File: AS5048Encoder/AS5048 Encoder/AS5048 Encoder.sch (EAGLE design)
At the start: 5 parts, among them X1 SI-50170

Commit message: all parts in place
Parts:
- added TP1, TP2, TP3, TP4, TP5: TPPAD1-17, testpad:TPPAD1-17
- added U$2: AS5145, makesmith:AS5145
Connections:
- new net N$10: X1.NC
- new net N$11: X1.C_GND
- new net N$2: U$2.CSN
- new net N$3: U$2.CLK
- new net N$4: U$2.DO
- new net N$9: X1.RD-
- new net SIG_A: TP4.TP, U$2.DTEST1A, X1.RD+
- new net SIG_B: TP5.TP, U$2.DTEST2B, X1.RCT
- net GND: now also TP2.TP
- net PWM: now also TP3.TP, U$2.PWM
- net VCC: now also TP1.TP
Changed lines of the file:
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@@
 <layer number="54" name="bGND_GNDA" color="1" fill="9" visible="no" active="no"/>
 <layer number="56" name="wert" color="7" fill="1" visible="no" active="no"/>
+<layer number="90" name="Modules" color="5" fill="1" visible="yes" active="yes"/>
 <layer number="91" name="Nets" color="2" fill="1" visible="yes" active="yes"/>
 <layer number="92" name="Busses" color="1" fill="1" visible="yes" active="yes"/>
@@
 <part name="U$1" library="austriamicrosystems" deviceset="AS5048" device=""/>
 <part name="X1" library="con-stewart" deviceset="SI-50170" device=""/>
+<part name="U$2" library="makesmith" deviceset="AS5145" device=""/>
+<part name="TP1" library="testpad" deviceset="TP" device="PAD1-17"/>
+<part name="TP2" library="testpad" deviceset="TP" device="PAD1-17"/>
+<part name="TP3" library="testpad" deviceset="TP" device="PAD1-17"/>
+<part name="TP4" library="testpad" deviceset="TP" device="PAD1-17"/>
+<part name="TP5" library="testpad" deviceset="TP" device="PAD1-17"/>
 </parts>
 <sheets>
@@
 <instance part="U$1" gate="G$1" x="66.04" y="25.4"/>
 <instance part="X1" gate="G$1" x="66.04" y="-7.62"/>
+<instance part="U$2" gate="G$1" x="-43.18" y="12.7"/>
+<instance part="TP1" gate="G$1" x="-38.1" y="63.5"/>
+<instance part="TP2" gate="G$1" x="-25.4" y="63.5"/>
+<instance part="TP3" gate="G$1" x="-12.7" y="63.5"/>
+<instance part="TP4" gate="G$1" x="-2.54" y="63.5"/>
+<instance part="TP5" gate="G$1" x="5.08" y="63.5"/>
 </instances>
 <busses>
@@
 <label x="48.26" y="2.54" size="1.778" layer="95"/>
 </segment>
+<segment>
+<pinref part="TP2" gate="G$1" pin="TP"/>
+<wire x1="-25.4" y1="60.96" x2="-25.4" y2="55.88" width="0.1524" layer="91"/>
+<label x="-25.4" y="55.88" size="1.778" layer="95" rot="R90"/>
+</segment>
 </net>
 <net name="VCC" class="0">
@@
 <label x="48.26" y="7.62" size="1.778" layer="95"/>
 </segment>
+<segment>
+<pinref part="TP1" gate="G$1" pin="TP"/>
+<wire x1="-38.1" y1="60.96" x2="-38.1" y2="55.88" width="0.1524" layer="91"/>
+<label x="-38.1" y="55.88" size="1.778" layer="95" rot="R90"/>
+</segment>
 </net>
 <net name="3V3" class="0">
@@
 <label x="48.26" y="5.08" size="1.778" layer="95"/>
 </segment>
-</net>
+<segment>
+<pinref part="U$2" gate="G$1" pin="PWM"/>
+<wire x1="-17.78" y1="5.08" x2="-12.7" y2="5.08" width="0.1524" layer="91"/>
+<label x="-12.7" y="5.08" size="1.778" layer="95"/>
+</segment>
+<segment>
+<pinref part="TP3" gate="G$1" pin="TP"/>
+<wire x1="-12.7" y1="60.96" x2="-12.7" y2="55.88" width="0.1524" layer="91"/>
+<label x="-12.7" y="55.88" size="1.778" layer="95" rot="R90"/>
+</segment>
+</net>
+<net name="N$2" class="0">
+<segment>
+<pinref part="U$2" gate="G$1" pin="CSN"/>
+<wire x1="-17.78" y1="0" x2="-12.7" y2="0" width="0.1524" layer="91"/>
+</segment>
+</net>
+<net name="N$3" class="0">
+<segment>
+<pinref part="U$2" gate="G$1" pin="CLK"/>
+<wire x1="-17.78" y1="-5.08" x2="-12.7" y2="-5.08" width="0.1524" layer="91"/>
+</segment>
+</net>
+<net name="N$4" class="0">
+<segment>
+<pinref part="U$2" gate="G$1" pin="DO"/>
+<wire x1="-17.78" y1="-10.16" x2="-12.7" y2="-10.16" width="0.1524" layer="91"/>
+</segment>
+</net>
+<net name="SIG_A" class="0">
+<segment>
+<pinref part="U$2" gate="G$1" pin="DTEST1A"/>
+<wire x1="-63.5" y1="15.24" x2="-68.58" y2="15.24" width="0.1524" layer="91"/>
+<label x="-73.66" y="15.24" size="1.778" layer="95"/>
+</segment>
+<segment>
+<pinref part="X1" gate="G$1" pin="RD+"/>
+<wire x1="55.88" y1="0" x2="53.34" y2="0" width="0.1524" layer="91"/>
+<label x="45.72" y="0" size="1.778" layer="95"/>
+</segment>
+<segment>
+<pinref part="TP4" gate="G$1" pin="TP"/>
+<wire x1="-2.54" y1="60.96" x2="-2.54" y2="55.88" width="0.1524" layer="91"/>
+<label x="-2.54" y="53.34" size="1.778" layer="95" rot="R90"/>
+</segment>
+</net>
+<net name="SIG_B" class="0">
+<segment>
+<pinref part="U$2" gate="G$1" pin="DTEST2B"/>
+<wire x1="-63.5" y1="10.16" x2="-68.58" y2="10.16" width="0.1524" layer="91"/>
+<label x="-73.66" y="10.16" size="1.778" layer="95"/>
+</segment>
+<segment>
+<pinref part="X1" gate="G$1" pin="RCT"/>
+<wire x1="55.88" y1="-2.54" x2="53.34" y2="-2.54" width="0.1524" layer="91"/>
+<label x="45.72" y="-2.54" size="1.778" layer="95"/>
+</segment>
+<segment>
+<pinref part="TP5" gate="G$1" pin="TP"/>
+<wire x1="5.08" y1="60.96" x2="5.08" y2="55.88" width="0.1524" layer="91"/>
+<label x="5.08" y="53.34" size="1.778" layer="95" rot="R90"/>
+</segment>
+</net>
+<net name="N$9" class="0">
+<segment>
+<pinref part="X1" gate="G$1" pin="RD-"/>
+<wire x1="55.88" y1="-5.08" x2="53.34" y2="-5.08" width="0.1524" layer="91"/>
+</segment>
+</net>
+<net name="N$10" class="0">
+<segment>
+<pinref part="X1" gate="G$1" pin="NC"/>
+<wire x1="55.88" y1="-7.62" x2="53.34" y2="-7.62" width="0.1524" layer="91"/>
+</segment>
+</net>
+<net name="N$11" class="0">
+<segment>
+<pinref part="X1" gate="G$1" pin="C_GND"/>
+<wire x1="55.88" y1="-10.16" x2="53.34" y2="-10.16" width="0.1524" layer="91"/>
+</segment>
+</net>

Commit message: board looks done?
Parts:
- removed U$1: AS5048, austriamicrosystems:AS5048
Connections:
- removed net N$10: X1.NC
- removed net N$11: X1.C_GND
- removed net N$9: X1.RD-
- net 3V3: now also U$2.VDD3V3; no longer U$1.3V3
- net GND: now also X1.NC; no longer U$1.GND, X1.TD-
- net PWM: now also X1.C_GND; no longer U$1.PWM, X1.TCT
- net SIG_A: now also X1.TCT; no longer X1.RD+
- net SIG_B: now also X1.TD+; no longer X1.RCT
- net VCC: now also U$2.VDD5V, X1.RD-; no longer U$1.5V, X1.TD+
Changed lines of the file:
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@@
 <part name="SUPPLY6" library="SparkFun-Aesthetics" deviceset="VCC" device=""/>
 <part name="JP1" library="SparkFun-Connectors" deviceset="M03" device="LOCK"/>
-<part name="U$1" library="austriamicrosystems" deviceset="AS5048" device=""/>
 <part name="X1" library="con-stewart" deviceset="SI-50170" device=""/>
 <part name="U$2" library="makesmith" deviceset="AS5145" device=""/>
@@
 <instance part="SUPPLY6" gate="1" x="12.7" y="27.94"/>
 <instance part="JP1" gate="G$1" x="63.5" y="58.42" rot="R270"/>
-<instance part="U$1" gate="G$1" x="66.04" y="25.4"/>
 <instance part="X1" gate="G$1" x="66.04" y="-7.62"/>
 <instance part="U$2" gate="G$1" x="-43.18" y="12.7"/>
@@
 </segment>
 <segment>
-<wire x1="53.34" y1="20.32" x2="50.8" y2="20.32" width="0.1524" layer="91"/>
-<label x="45.72" y="20.32" size="1.778" layer="95"/>
-<pinref part="U$1" gate="G$1" pin="GND"/>
-</segment>
-<segment>
 <pinref part="JP1" gate="G$1" pin="1"/>
 <wire x1="60.96" y1="50.8" x2="60.96" y2="45.72" width="0.1524" layer="91"/>
@@
 </segment>
 <segment>
-<pinref part="X1" gate="G$1" pin="TD-"/>
-<wire x1="55.88" y1="2.54" x2="53.34" y2="2.54" width="0.1524" layer="91"/>
-<label x="48.26" y="2.54" size="1.778" layer="95"/>
-</segment>
-<segment>
 <pinref part="TP2" gate="G$1" pin="TP"/>
 <wire x1="-25.4" y1="60.96" x2="-25.4" y2="55.88" width="0.1524" layer="91"/>
 <label x="-25.4" y="55.88" size="1.778" layer="95" rot="R90"/>
+</segment>
+<segment>
+<pinref part="X1" gate="G$1" pin="NC"/>
+<wire x1="55.88" y1="-7.62" x2="53.34" y2="-7.62" width="0.1524" layer="91"/>
+<label x="48.26" y="-7.62" size="1.778" layer="95"/>
 </segment>
 </net>
@@
 </segment>
 <segment>
-<wire x1="53.34" y1="30.48" x2="50.8" y2="30.48" width="0.1524" layer="91"/>
-<label x="45.72" y="30.48" size="1.778" layer="95"/>
-<pinref part="U$1" gate="G$1" pin="5V"/>
-</segment>
-<segment>
 <pinref part="JP1" gate="G$1" pin="2"/>
 <wire x1="63.5" y1="50.8" x2="63.5" y2="45.72" width="0.1524" layer="91"/>
@@
 </segment>
 <segment>
-<pinref part="X1" gate="G$1" pin="TD+"/>
-<wire x1="55.88" y1="7.62" x2="53.34" y2="7.62" width="0.1524" layer="91"/>
-<label x="48.26" y="7.62" size="1.778" layer="95"/>
-</segment>
-<segment>
 <pinref part="TP1" gate="G$1" pin="TP"/>
 <wire x1="-38.1" y1="60.96" x2="-38.1" y2="55.88" width="0.1524" layer="91"/>
 <label x="-38.1" y="55.88" size="1.778" layer="95" rot="R90"/>
+</segment>
+<segment>
+<pinref part="U$2" gate="G$1" pin="VDD5V"/>
+<wire x1="-17.78" y1="25.4" x2="-15.24" y2="25.4" width="0.1524" layer="91"/>
+<label x="-15.24" y="25.4" size="1.778" layer="95"/>
+</segment>
+<segment>
+<pinref part="X1" gate="G$1" pin="RD-"/>
+<wire x1="55.88" y1="-5.08" x2="53.34" y2="-5.08" width="0.1524" layer="91"/>
+<label x="48.26" y="-5.08" size="1.778" layer="95"/>
 </segment>
 </net>
@@
 </segment>
 <segment>
-<wire x1="53.34" y1="25.4" x2="50.8" y2="25.4" width="0.1524" layer="91"/>
-<label x="45.72" y="25.4" size="1.778" layer="95"/>
-<pinref part="U$1" gate="G$1" pin="3V3"/>
+<pinref part="U$2" gate="G$1" pin="VDD3V3"/>
+<wire x1="-17.78" y1="20.32" x2="-15.24" y2="20.32" width="0.1524" layer="91"/>
+<label x="-15.24" y="20.32" size="1.778" layer="95"/>
 </segment>
 </net>
 <net name="PWM" class="0">
 <segment>
-<label x="83.82" y="27.94" size="1.778" layer="95"/>
-<pinref part="U$1" gate="G$1" pin="PWM"/>
-<wire x1="81.28" y1="27.94" x2="83.82" y2="27.94" width="0.1524" layer="91"/>
-</segment>
-<segment>
 <pinref part="JP1" gate="G$1" pin="3"/>
 <wire x1="66.04" y1="50.8" x2="66.04" y2="45.72" width="0.1524" layer="91"/>
 <label x="66.04" y="40.64" size="1.778" layer="95" rot="R90"/>
-</segment>
-<segment>
-<pinref part="X1" gate="G$1" pin="TCT"/>
-<wire x1="55.88" y1="5.08" x2="53.34" y2="5.08" width="0.1524" layer="91"/>
-<label x="48.26" y="5.08" size="1.778" layer="95"/>
 </segment>
 <segment>
@@
 <wire x1="-12.7" y1="60.96" x2="-12.7" y2="55.88" width="0.1524" layer="91"/>
 <label x="-12.7" y="55.88" size="1.778" layer="95" rot="R90"/>
+</segment>
+<segment>
+<pinref part="X1" gate="G$1" pin="C_GND"/>
+<wire x1="55.88" y1="-10.16" x2="53.34" y2="-10.16" width="0.1524" layer="91"/>
+<label x="48.26" y="-10.16" size="1.778" layer="95"/>
 </segment>
 </net>
@@
 </segment>
 <segment>
-<pinref part="X1" gate="G$1" pin="RD+"/>
-<wire x1="55.88" y1="0" x2="53.34" y2="0" width="0.1524" layer="91"/>
-<label x="45.72" y="0" size="1.778" layer="95"/>
-</segment>
-<segment>
 <pinref part="TP4" gate="G$1" pin="TP"/>
 <wire x1="-2.54" y1="60.96" x2="-2.54" y2="55.88" width="0.1524" layer="91"/>
 <label x="-2.54" y="53.34" size="1.778" layer="95" rot="R90"/>
+</segment>
+<segment>
+<pinref part="X1" gate="G$1" pin="TCT"/>
+<wire x1="55.88" y1="5.08" x2="53.34" y2="5.08" width="0.1524" layer="91"/>
+<label x="45.72" y="5.08" size="1.778" layer="95"/>
 </segment>
 </net>
@@
 </segment>
 <segment>
-<pinref part="X1" gate="G$1" pin="RCT"/>
-<wire x1="55.88" y1="-2.54" x2="53.34" y2="-2.54" width="0.1524" layer="91"/>
-<label x="45.72" y="-2.54" size="1.778" layer="95"/>
-</segment>
-<segment>
 <pinref part="TP5" gate="G$1" pin="TP"/>
 <wire x1="5.08" y1="60.96" x2="5.08" y2="55.88" width="0.1524" layer="91"/>
 <label x="5.08" y="53.34" size="1.778" layer="95" rot="R90"/>
 </segment>
-</net>
-<net name="N$9" class="0">
 <segment>
-<pinref part="X1" gate="G$1" pin="RD-"/>
-<wire x1="55.88" y1="-5.08" x2="53.34" y2="-5.08" width="0.1524" layer="91"/>
+<pinref part="X1" gate="G$1" pin="TD+"/>
+<wire x1="55.88" y1="7.62" x2="53.34" y2="7.62" width="0.1524" layer="91"/>
+<label x="45.72" y="7.62" size="1.778" layer="95"/>
 </segment>
 </net>
-<net name="N$10" class="0">
-<segment>
-<pinref part="X1" gate="G$1" pin="NC"/>
-<wire x1="55.88" y1="-7.62" x2="53.34" y2="-7.62" width="0.1524" layer="91"/>
-</segment>
-</net>
-<net name="N$11" class="0">
-<segment>
-<pinref part="X1" gate="G$1" pin="C_GND"/>
-<wire x1="55.88" y1="-10.16" x2="53.34" y2="-10.16" width="0.1524" layer="91"/>
-</segment>
-</net>

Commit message: routed mode
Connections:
- new net MODE_INDEX: U$2.MODE_INDEX, X1.TD-
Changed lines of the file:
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@@
+</segment>
+</net>
+<net name="MODE_INDEX" class="0">
+<segment>
+<pinref part="U$2" gate="G$1" pin="MODE_INDEX"/>
+<wire x1="-63.5" y1="0" x2="-68.58" y2="0" width="0.1524" layer="91"/>
+<label x="-83.82" y="0" size="1.778" layer="95"/>
+</segment>
+<segment>
+<pinref part="X1" gate="G$1" pin="TD-"/>
+<wire x1="55.88" y1="2.54" x2="53.34" y2="2.54" width="0.1524" layer="91"/>
+<label x="38.1" y="2.54" size="1.778" layer="95"/>
 </segment>
 </net>

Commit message: added ground connection
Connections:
- net GND: now also U$2.VSS
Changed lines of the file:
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@@
 <label x="48.26" y="-7.62" size="1.778" layer="95"/>
+</segment>
+<segment>
+<pinref part="U$2" gate="G$1" pin="VSS"/>
+<wire x1="-63.5" y1="-5.08" x2="-68.58" y2="-5.08" width="0.1524" layer="91"/>
+<label x="-73.66" y="-5.08" size="1.778" layer="95"/>
 </segment>
 </net>

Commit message: cns low
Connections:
- removed net N$2: U$2.CSN
- net GND: now also U$2.CSN
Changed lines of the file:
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@@
 <label x="-73.66" y="-5.08" size="1.778" layer="95"/>
+</segment>
+<segment>
+<pinref part="U$2" gate="G$1" pin="CSN"/>
+<wire x1="-17.78" y1="0" x2="-12.7" y2="0" width="0.1524" layer="91"/>
+<label x="-12.7" y="0" size="1.778" layer="95"/>
 </segment>
 </net>
@@
 </segment>
 </net>
-<net name="N$2" class="0">
-<segment>
-<pinref part="U$2" gate="G$1" pin="CSN"/>
-<wire x1="-17.78" y1="0" x2="-12.7" y2="0" width="0.1524" layer="91"/>
-</segment>
-</net>

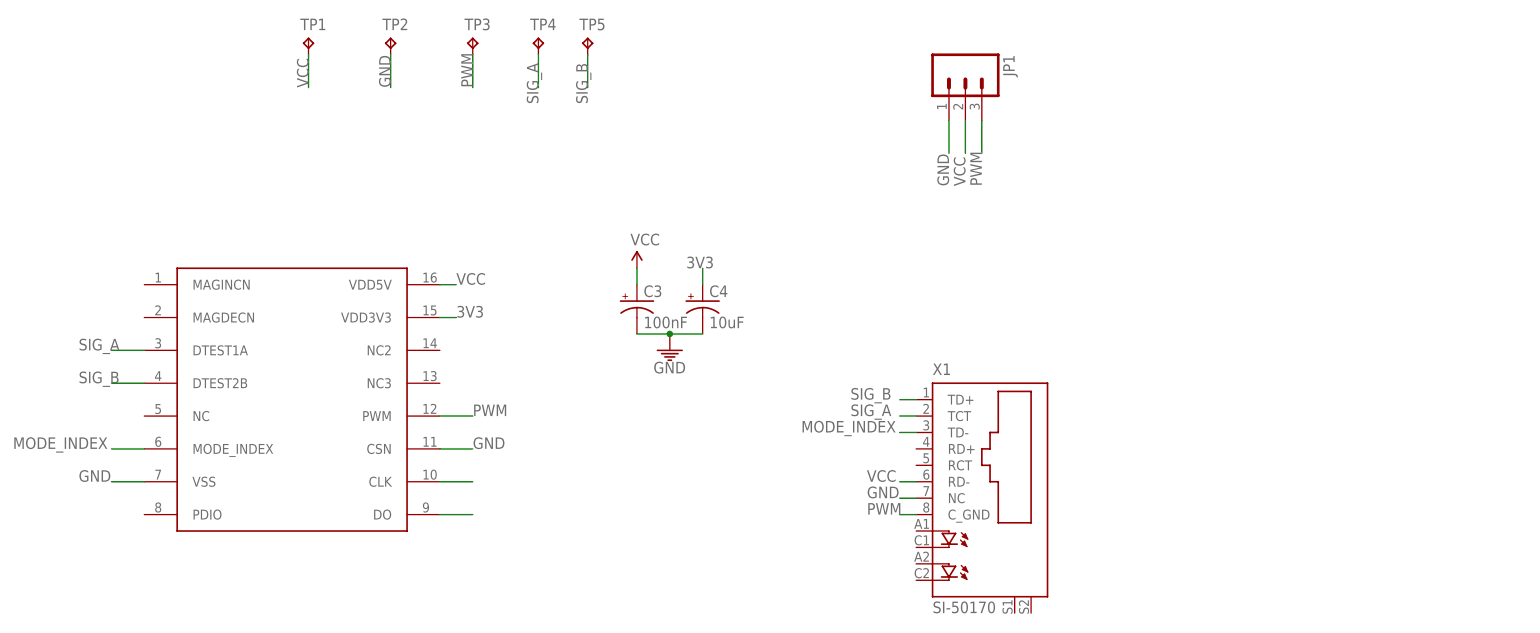
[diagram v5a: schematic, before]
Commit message: total revamp of encoder board
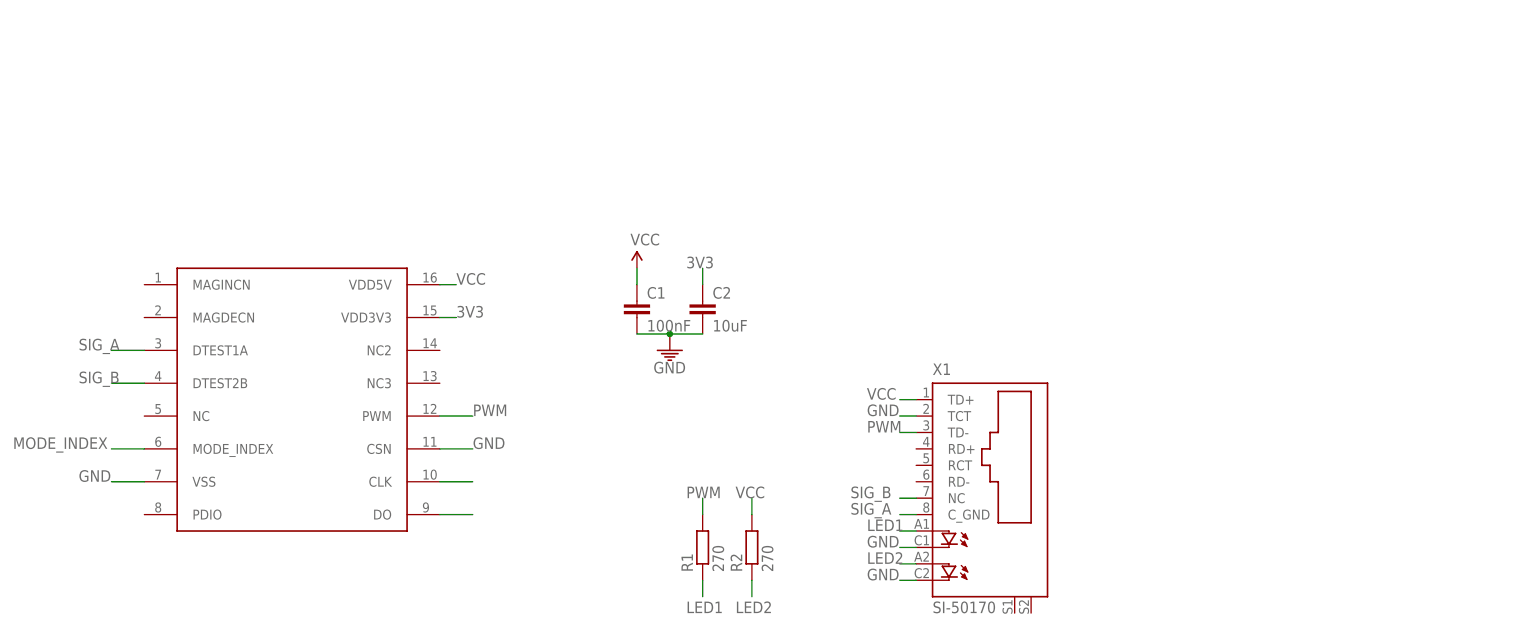
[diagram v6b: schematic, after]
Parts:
- removed C3: 100nF, SparkFun-Passives:CAP_POL1206-KIT
- removed C4: 10uF, SparkFun-Passives:CAP_POL1206-KIT
- removed JP1: (no value), SparkFun-Connectors:M03LOCK
- removed TP1, TP2, TP3, TP4, TP5: TPPAD1-17, testpad:TPPAD1-17
- added C1: 100nF, eagle-ltspice:C
- added C2: 10uF, eagle-ltspice:C
- added R1, R2: 270, eagle-ltspice:R
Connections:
- new net LED1: R1.1, X1.A
- new net LED2: R2.1, X1.A1
- net 3V3: now also C2.1; no longer C4.+
- net GND: now also C1.2, C2.2, X1.C, X1.C1, X1.TCT; no longer C3.-, C4.-, JP1.1, TP2.TP, X1.NC
- net MODE_INDEX: no longer X1.TD-
- net PWM: now also R1.2, X1.TD-; no longer JP1.3, TP3.TP, X1.C_GND
- net SIG_A: now also X1.C_GND; no longer TP4.TP, X1.TCT
- net SIG_B: now also X1.NC; no longer TP5.TP, X1.TD+
- net VCC: now also C1.1, R2.2, X1.TD+; no longer C3.+, JP1.2, TP1.TP, X1.RD-

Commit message: add todo list
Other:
- note added: "To Do: Add cut outs for accessing lower screws without removing upper board"
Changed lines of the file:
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@@
 <sheet>
 <plain>
+<text x="45.72" y="45.72" size="1.778" layer="97">To Do:
+Add cut outs for accessing lower screws without removing upper board</text>
 </plain>
 <instances>
@@
 </schematic>
 </drawing>
+<compatibility>
+<note version="6.3" minversion="6.2.2" severity="warning">
+Since Version 6.2.2 text objects can contain more than one line,
+which will not be processed correctly with this version.
+</note>
+</compatibility>
 </eagle>
